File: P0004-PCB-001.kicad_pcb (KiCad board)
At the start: 2 copper layers, 63.5 x 38.5 mm, 104 parts, among them CN1 104031-0811, CN2 Liansheng PH--00603, CN3 Molex 105057-0001, CN4 Samtec FTSH-107-01-L-DV-K, CN5 M20-9990346, SW1 Khon TSB06331-090D332DA-R0500, SW2 Khon TSB06331-090D332DA-R0500, SW3 Khon TSB06331-090D332DA-R0500, SW4 Khon TSB06331-090D332DA-R0500, U1 W5500, U2 TMP102AIDRL, U3 Microchip 24AA256UIDT-I/ST, U4 STM32H743VIT6, U5 TI LMR54410DBV, U6 INA3221AIRGV

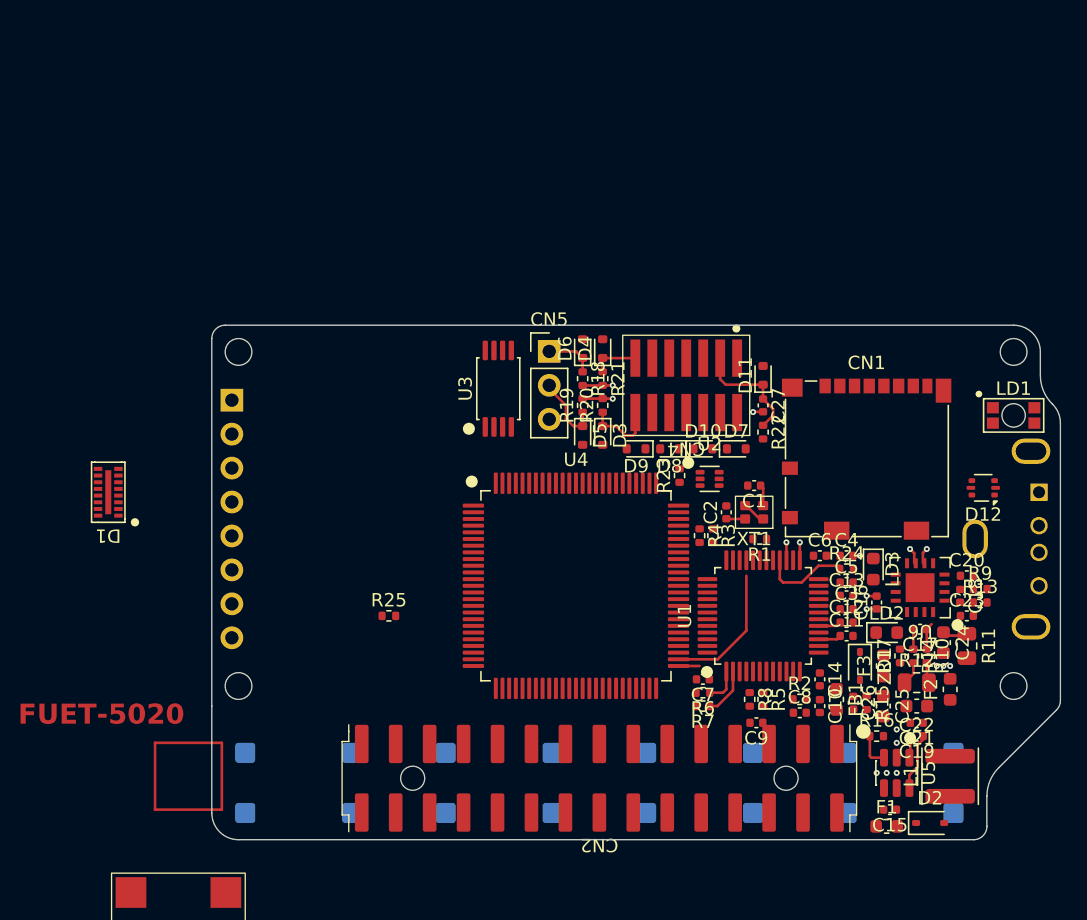
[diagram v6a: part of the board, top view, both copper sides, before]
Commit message: added 5v regulator
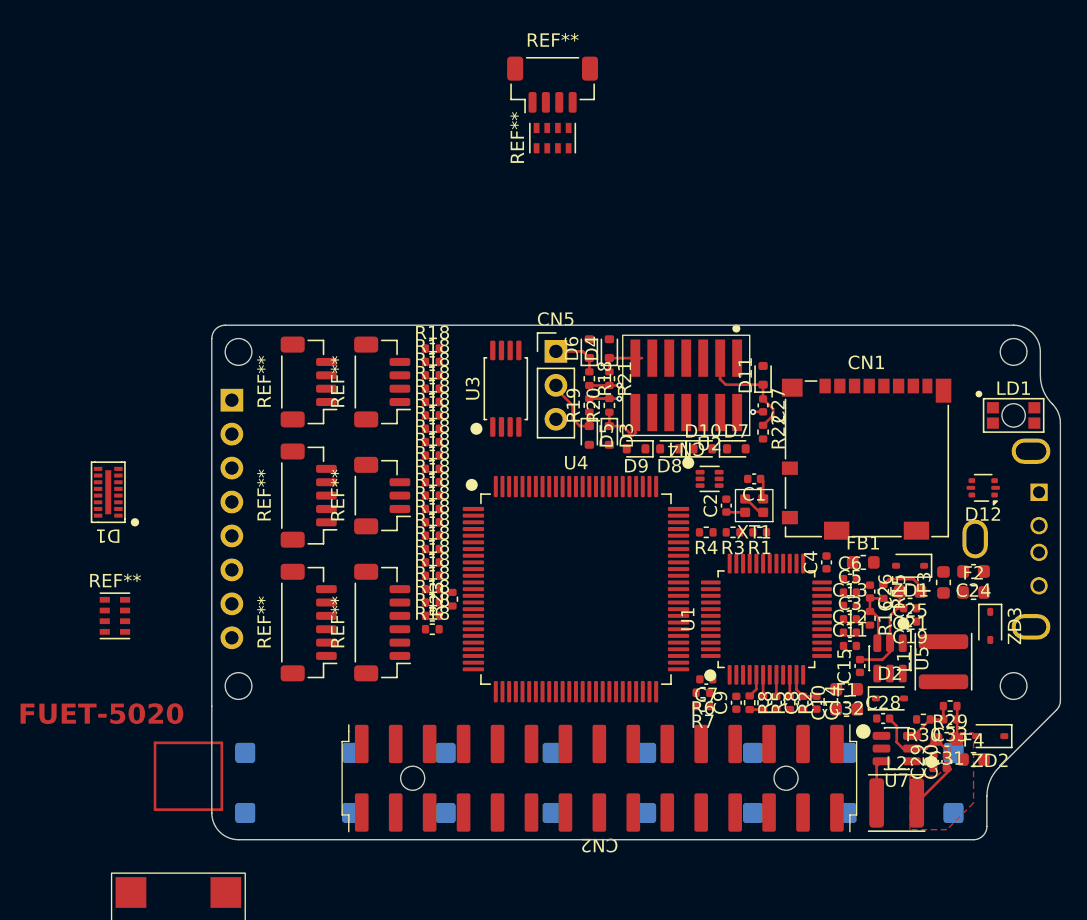
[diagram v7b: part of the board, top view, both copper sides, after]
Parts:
- removed C16, C17, C18, C20, C23: 100n, Capacitor_WUT:C_0402_1005Metric
- removed C22: 22u, Capacitor_SMD:C_0603_1608Metric
- removed LD2: Green, LED_SMD:LED_0603_1608Metric
- removed LD3: Red, LED_SMD:LED_0603_1608Metric
- removed R10, R13, R14, R9: 100R, Resistor_WUT:R_0402_1005Metric
- removed R11, R12: 150m, Resistor_SMD:R_0805_2012Metric
- removed R17, R24: 1k0, Resistor_WUT:R_0402_1005Metric
- removed R25: 10k, Resistor_WUT:R_0402_1005Metric
- removed U6: INA3221AIRGV, IC_WUT:Texas_VQFN-16-1EP_RGV0016A
- added C28: 2u2, Capacitor_WUT:C_0402_1005Metric, F.Cu at (194.2, 114.9)
- added C29: 100n, Capacitor_WUT:C_0402_1005Metric, F.Cu at (198.0, 118.2)
- added C30: 100n, Capacitor_WUT:C_0402_1005Metric, F.Cu at (199.0, 118.2)
- added C31: 22u, Capacitor_SMD:C_0603_1608Metric, F.Cu at (199.0, 116.5)
- added C32: 22u, Capacitor_SMD:C_0603_1608Metric, F.Cu at (191.5, 112.8)
- added C33: 15p, Capacitor_WUT:C_0402_1005Metric, F.Cu at (199.2, 115.0)
- added F4: 1A, Fuse:Fuse_0603_1608Metric, F.Cu at (201.0, 118.0)
- added L2: 10u, Inductor_WUT:APV_ANR4030, F.Cu at (195.2, 121.2)
- added R18: 100R, Resistor_WUT:R_0402_1005Metric, F.Cu at (160.5, 103.2)
- added R18: 100R, Resistor_WUT:R_0402_1005Metric, F.Cu at (160.5, 102.2)
- added R18: 100R, Resistor_WUT:R_0402_1005Metric, F.Cu at (160.5, 91.2)
- added R18: 100R, Resistor_WUT:R_0402_1005Metric, F.Cu at (160.5, 98.2)
- added R18: 100R, Resistor_WUT:R_0402_1005Metric, F.Cu at (160.5, 106.2)
- added R18: 100R, Resistor_WUT:R_0402_1005Metric, F.Cu at (160.5, 94.2)
- added R18: 100R, Resistor_WUT:R_0402_1005Metric, F.Cu at (160.5, 97.2)
- added R18: 100R, Resistor_WUT:R_0402_1005Metric, F.Cu at (160.5, 104.2)
- added R18: 100R, Resistor_WUT:R_0402_1005Metric, F.Cu at (160.5, 105.2)
- added R18: 100R, Resistor_WUT:R_0402_1005Metric, F.Cu at (160.5, 107.2)
- added R18: 100R, Resistor_WUT:R_0402_1005Metric, F.Cu at (160.5, 101.2)
- added R18: 100R, Resistor_WUT:R_0402_1005Metric, F.Cu at (160.5, 93.2)
- added R18: 100R, Resistor_WUT:R_0402_1005Metric, F.Cu at (160.5, 108.2)
- added R18: 100R, Resistor_WUT:R_0402_1005Metric, F.Cu at (160.5, 87.2)
- added R18: 100R, Resistor_WUT:R_0402_1005Metric, F.Cu at (160.5, 88.2)
- added R18: 100R, Resistor_WUT:R_0402_1005Metric, F.Cu at (160.5, 100.2)
- added R18: 100R, Resistor_WUT:R_0402_1005Metric, F.Cu at (160.5, 92.2)
- added R18: 100R, Resistor_WUT:R_0402_1005Metric, F.Cu at (160.5, 95.2)
- added R18: 100R, Resistor_WUT:R_0402_1005Metric, F.Cu at (160.5, 89.2)
- added R18: 100R, Resistor_WUT:R_0402_1005Metric, F.Cu at (160.5, 99.2)
- added R18: 100R, Resistor_WUT:R_0402_1005Metric, F.Cu at (160.5, 90.2)
- added R18: 100R, Resistor_WUT:R_0402_1005Metric, F.Cu at (160.5, 96.2)
- added R29: 47k, Resistor_WUT:R_0402_1005Metric, F.Cu at (199.2, 114.0)
- added R30: 15k, Resistor_WUT:R_0402_1005Metric, F.Cu at (197.2, 115.0)
- added REF**: JST_SH_BM04B-SRSS-TB_1x04-1MP_P1.00mm_Vertical, Connector_JST:JST_SH_BM04B-SRSS-TB_1x04-1MP_P1.00mm_Vertical, F.Cu at (151.2, 89.8)
- added REF**: JST_SH_BM04B-SRSS-TB_1x04-1MP_P1.00mm_Vertical, Connector_JST:JST_SH_BM04B-SRSS-TB_1x04-1MP_P1.00mm_Vertical, F.Cu at (156.8, 89.8)
- added REF**: JST_SH_BM06B-SRSS-TB_1x06-1MP_P1.00mm_Vertical, Connector_JST:JST_SH_BM06B-SRSS-TB_1x06-1MP_P1.00mm_Vertical, F.Cu at (151.2, 107.8)
- added REF**: JST_SH_BM05B-SRSS-TB_1x05-1MP_P1.00mm_Vertical, Connector_JST:JST_SH_BM05B-SRSS-TB_1x05-1MP_P1.00mm_Vertical, F.Cu at (151.2, 98.2)
- added REF**: R_Cat16-4, Resistor_SMD:R_Cat16-4, F.Cu at (169.5, 71.5)
- added REF**: JST_SH_BM04B-SRSS-TB_1x04-1MP_P1.00mm_Vertical, Connector_JST:JST_SH_BM04B-SRSS-TB_1x04-1MP_P1.00mm_Vertical, F.Cu at (169.5, 67.5)
- added REF**: JST_SH_BM06B-SRSS-TB_1x06-1MP_P1.00mm_Vertical, Connector_JST:JST_SH_BM06B-SRSS-TB_1x06-1MP_P1.00mm_Vertical, F.Cu at (156.8, 107.8)
- added REF**: JST_SH_BM03B-SRSS-TB_1x03-1MP_P1.00mm_Vertical, Connector_JST:JST_SH_BM03B-SRSS-TB_1x03-1MP_P1.00mm_Vertical, F.Cu at (156.8, 98.2)
- added REF**: R_Cat16-4, Resistor_SMD:R_Cat16-4, F.Cu at (136.8, 107.2)
- added U7: TI LMR54410DBV, IC_WUT:SOT-23-6, F.Cu at (195.2, 117.2)
- added ZD2: 3V3, Diode_SMD:D_SOD-323, F.Cu at (202.2, 116.2)
- added ZD3: 3V3, Diode_SMD:D_SOD-323, F.Cu at (202.2, 108.0)
- moved R23 19.4 mm to (162.0, 106.0)
- moved C15 11.0 mm to (192.5, 111.0), turned to 90 degrees
- moved FB1 10.4 mm to (192.8, 103.2), turned to 0 degrees
- moved D2 9.79 mm to (194.8, 113.4)
- moved F1 9.25 mm to (191.5, 114.2)
- moved R16 8.83 mm to (193.2, 107.4), turned to -90 degrees
- moved C25 8.80 mm to (196.2, 105.4), turned to 180 degrees
- moved C19 8.58 mm to (196.2, 107.7)
- moved C21 8.58 mm to (196.2, 106.7)
- moved L1 8.58 mm to (198.8, 110.7)
- moved U5 8.58 mm to (194.8, 110.4)
- moved C26 8.41 mm to (193.2, 105.4)
- moved R15 8.41 mm to (194.2, 105.4)
- moved ZD1 8.39 mm to (196.2, 103.5), turned to 180 degrees
- moved F3 7.70 mm to (198.8, 104.8)
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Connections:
- net Net-(D2-K) renamed /Power Supplies/VIN_SAFE
- C25 pad 1: Net-(C25-Pad1) -> /Power Supplies/VOUT
- C26 pad 1: Net-(C25-Pad1) -> /Power Supplies/VOUT
- C26 pad 2: 0V -> Net-(U5-FB)
- F2 pad 2: Net-(F2-Pad2) -> /Power Supplies/3V3_EXPANSION
- F3 pad 1: Net-(C25-Pad1) -> /Power Supplies/VOUT
- R15 pad 1: Net-(C25-Pad1) -> /Power Supplies/VOUT
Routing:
- net 0V: track 3.01 -> 17.3 mm, vias 10 -> 1
- net /Microcontroller/ETH_PHY_SCK: track 10.1 -> 0.00 mm
- net 3V3: track 6.68 -> 0.00 mm
- net /Power Supplies/VOUT_5V: track 0.00 -> 6.14 mm
- net /Power Supplies/SW: track 4.31 -> 0.00 mm
- net Net-(U7-FB): track 0.00 -> 3.90 mm
- net /Power Supplies/SW_5V: track 0.00 -> 3.27 mm
- net Net-(U1-TXP): track 3.14 -> 0.00 mm
- net Net-(U1-TXN): track 2.18 -> 0.00 mm
- net Net-(U5-FB): track 2.60 -> 4.78 mm
- net /Power Supplies/VINT_SENSE_P: track 2.04 -> 0.00 mm
- net /Power Supplies/VOUT: track 1.56 -> 3.57 mm
- net /Power Supplies/3V3_EXPANSION: track 1.81 -> 0.00 mm
- net /Ethernet/ETH_RX_P: track 0.00 -> 1.78 mm
- net Net-(C25-Pad1): track 1.76 -> 0.00 mm
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- added copper zone on F.Cu, net /Power Supplies/VOUT_5V

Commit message: helps if you save first
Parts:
- removed C24: 22u, Capacitor_SMD:C_0603_1608Metric
- removed F4: 1A, Fuse:Fuse_0603_1608Metric
- removed the R18 at (160.5, 103.2)
- removed the R18 at (160.5, 102.2)
- removed the R18 at (160.5, 91.2)
- removed the R18 at (160.5, 98.2)
- removed the R18 at (160.5, 106.2)
- removed the R18 at (160.5, 94.2)
- removed the R18 at (160.5, 97.2)
- removed the R18 at (160.5, 104.2)
- removed the R18 at (160.5, 105.2)
- removed the R18 at (160.5, 107.2)
- removed the R18 at (160.5, 101.2)
- removed the R18 at (160.5, 93.2)
- removed the R18 at (160.5, 108.2)
- removed the R18 at (160.5, 87.2)
- removed the R18 at (160.5, 88.2)
- removed the R18 at (160.5, 100.2)
- removed the R18 at (160.5, 92.2)
- removed the R18 at (160.5, 95.2)
- removed the R18 at (160.5, 89.2)
- removed the R18 at (160.5, 99.2)
- removed the R18 at (160.5, 90.2)
- removed the R18 at (160.5, 96.2)
- removed REF** (x3): JST_SH_BM04B-SRSS-TB_1x04-1MP_P1.00mm_Vertical, Connector_JST:JST_SH_BM04B-SRSS-TB_1x04-1MP_P1.00mm_Vertical
- removed REF** (x2): JST_SH_BM06B-SRSS-TB_1x06-1MP_P1.00mm_Vertical, Connector_JST:JST_SH_BM06B-SRSS-TB_1x06-1MP_P1.00mm_Vertical
- removed REF**: JST_SH_BM05B-SRSS-TB_1x05-1MP_P1.00mm_Vertical, Connector_JST:JST_SH_BM05B-SRSS-TB_1x05-1MP_P1.00mm_Vertical
- removed REF** (x2): R_Cat16-4, Resistor_SMD:R_Cat16-4
- removed REF**: JST_SH_BM03B-SRSS-TB_1x03-1MP_P1.00mm_Vertical, Connector_JST:JST_SH_BM03B-SRSS-TB_1x03-1MP_P1.00mm_Vertical
- removed ZD1, ZD2, ZD3: 3V3, Diode_SMD:D_SOD-323
- added C20: 47u, Capacitor_SMD:C_1206_3216Metric, F.Cu at (210.5, 96.0)
- added C22: 47u, Capacitor_SMD:C_1206_3216Metric, F.Cu at (211.8, 103.2)
- added C23: 47u, Capacitor_SMD:C_1206_3216Metric, F.Cu at (215.8, 112.4)
- added C34: 100n, Capacitor_WUT:C_0402_1005Metric, F.Cu at (199.8, 104.5)
- added D13: 5V, Diode_SMD:D_SOD-523, F.Cu at (219.5, 94.5)
- added D14: 5V, Diode_SMD:D_SOD-523, F.Cu at (196.2, 104.0)
- added R10: 10k, Resistor_WUT:R_0402_1005Metric, F.Cu at (201.8, 107.8)
- added R11: 10k, Resistor_WUT:R_0402_1005Metric, F.Cu at (216.0, 104.8)
- added R9: 47k, Resistor_WUT:R_0402_1005Metric, F.Cu at (202.8, 107.8)
- added U6: TI TPS2553DBV, IC_WUT:SOT-23-6, F.Cu at (202.5, 105.0)
- F2: value 250mA -> 1A
- moved FB1 29.8 mm to (211.8, 126.2)
- moved F3 12.3 mm to (201.2, 116.8)
- moved D12 9.02 mm to (210.5, 99.8)
- moved F2 2.61 mm to (198.5, 104.8), turned to 90 degrees
- moved C28 0.07 mm to (194.2, 115.0)
- moved C19 0.07 mm to (196.2, 107.8)
- moved C21 0.07 mm to (196.2, 106.8)
- moved C25 0.07 mm to (196.2, 105.5)
- moved C26 0.07 mm to (193.2, 105.5)
- moved C29 0.07 mm to (198.0, 118.2)
- moved C30 0.07 mm to (199.0, 118.2)
- moved D2 0.07 mm to (194.8, 113.5)
- moved L1 0.07 mm to (198.8, 110.8)
- moved R15 0.07 mm to (194.2, 105.5)
- moved R16 0.07 mm to (193.2, 107.5)
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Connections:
- C19 pad 1: /Power Supplies/SW -> /Power Supplies/SW_5V
- C21 pad 1: /Power Supplies/VOUT -> /Power Supplies/VOUT_5V
- C25 pad 1: /Power Supplies/VOUT -> /Power Supplies/VOUT_5V
- C26 pad 1: /Power Supplies/VOUT -> /Power Supplies/VOUT_5V
- C29 pad 1: /Power Supplies/SW_5V -> /Power Supplies/SW_3V3
- C30 pad 1: /Power Supplies/VOUT_5V -> /Power Supplies/VOUT_3V3
- C31 pad 1: /Power Supplies/VOUT_5V -> /Power Supplies/VOUT_3V3
- C33 pad 1: /Power Supplies/VOUT_5V -> /Power Supplies/VOUT_3V3
- CN3 pad 1: unconnected-(CN3-VBUS-Pad1) -> 5V_VBUS
- CN3 pad 2: unconnected-(CN3-D--Pad2) -> Net-(CN3-D-)
- CN3 pad 3: unconnected-(CN3-D+-Pad3) -> Net-(CN3-D+)
- D12 pad 1: unconnected-(D12-I/O1-Pad1) -> Net-(CN3-D+)
- D12 pad 3: unconnected-(D12-I/O2-Pad3) -> Net-(CN3-D-)
- F2 pad 1: /Power Supplies/VOUT -> /Power Supplies/VOUT_5V
- F2 pad 2: /Power Supplies/3V3_EXPANSION -> 5V
- F3 pad 1: /Power Supplies/VOUT -> /Power Supplies/VOUT_3V3
- L1 pad 1: /Power Supplies/SW -> /Power Supplies/SW_5V
- L1 pad 2: /Power Supplies/VOUT -> /Power Supplies/VOUT_5V
- L2 pad 1: /Power Supplies/SW_5V -> /Power Supplies/SW_3V3
- L2 pad 2: /Power Supplies/VOUT_5V -> /Power Supplies/VOUT_3V3
- R15 pad 1: /Power Supplies/VOUT -> /Power Supplies/VOUT_5V
- R29 pad 1: /Power Supplies/VOUT_5V -> /Power Supplies/VOUT_3V3
- U5 pad 6: /Power Supplies/SW -> /Power Supplies/SW_5V
- U7 pad 6: /Power Supplies/SW_5V -> /Power Supplies/SW_3V3
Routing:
- net /Power Supplies/VOUT_5V: track 6.14 -> 0.00 mm
- net /Power Supplies/VOUT_3V3: track 0.00 -> 6.14 mm
- net Net-(U1-XI/CLKIN): track 1.58 -> 7.08 mm
- net Net-(U1-XO): track 1.31 -> 5.70 mm
- net /Power Supplies/VOUT: track 3.57 -> 0.00 mm
- net /Power Supplies/SW_3V3: track 0.00 -> 3.27 mm
- net Net-(U5-CB): track 0.10 -> 1.74 mm
- net /Power Supplies/SW_5V: track 3.27 -> 4.31 mm
- added copper zone on F.Cu, net /Power Supplies/SW_5V
- added copper zone on F.Cu, net /Power Supplies/VOUT_3V3
